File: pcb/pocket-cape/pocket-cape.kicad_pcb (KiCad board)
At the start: 4 copper layers, 49 x 32.1 mm, 28 parts, among them J1 Sync1, J10 Display, J11 USB1, J2 12..16V, J3 Sync2, J4 Sled, J5 Laser1, J6 PM1, J7 PM2, J8 Laser2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

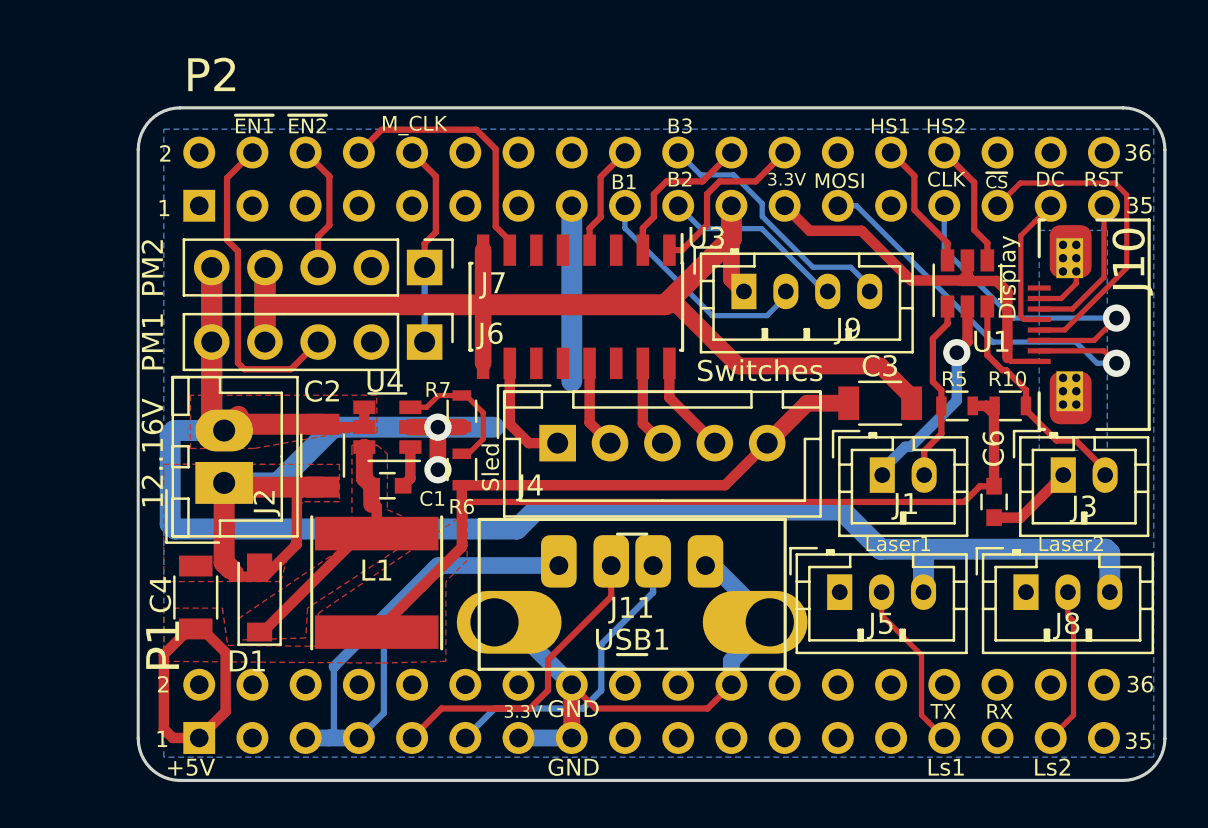
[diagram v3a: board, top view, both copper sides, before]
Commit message: Little tweaks (silk-screen; adding 100nF on 3.3V rail)
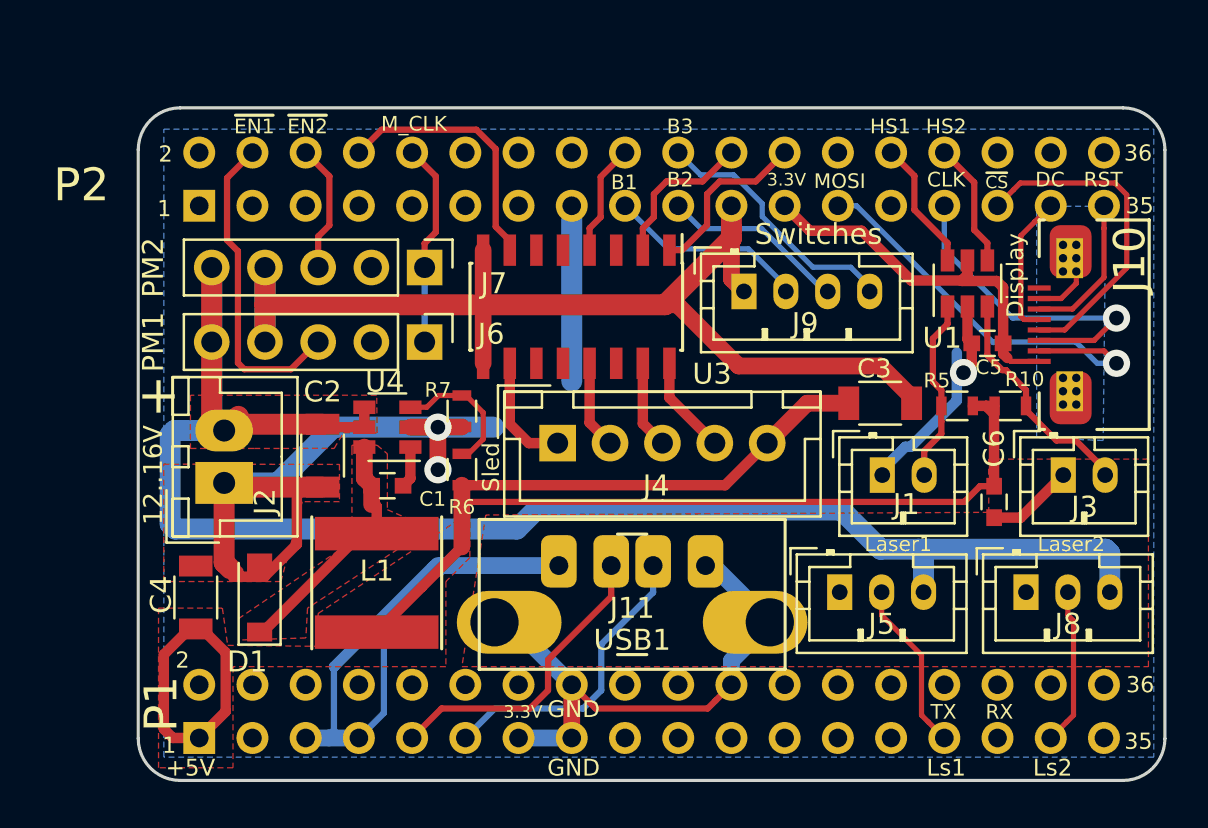
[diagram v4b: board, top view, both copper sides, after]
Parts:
- removed the REF*** at (148.5, 97.8)
- added C5: 100n, Capacitors_SMD:C_0603, F.Cu at (164.5, 100.1)
- added REF***: OSHW-Symbol_6.7x6mm_SilkScreen, Symbols:OSHW-Symbol_6.7x6mm_SilkScreen, B.Cu at (148.5, 97.9)
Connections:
- J10 pad 8: (no net) -> Net-(J10-Pad8)
- J6 pad 2: Net-(J6-Pad2) -> (no net)
- J7 pad 2: Net-(J7-Pad2) -> (no net)
- P1 pad 10: /(U1.B13)SPI0.MISO -> (no net)
- P1 pad 12: /(U1.B14)SPI0.MOSI -> (no net)
- P1 pad 14: (no net) -> Net-(P1-Pad14)
- P1 pad 17: /(U1.B9)VREF- -> (no net)
- P1 pad 18: /(U1.B7)VREF+ -> (no net)
- P1 pad 19: /(U1.A8)AIN0~1.8V -> (no net)
- P1 pad 2: /(U1.F2)AIN6~3.3V -> (no net)
- P1 pad 20: /(U1.B4)PRU-0.16 -> (no net)
- P1 pad 21: /(U1.B8)AIN1~1.8V -> (no net)
- P1 pad 23: /(U1.B6)AIN2~1.8V -> (no net)
- P1 pad 24: (no net) -> Net-(P1-Pad24)
- P1 pad 25: /(U1.C6)AIN3~1.8V -> (no net)
- P1 pad 26: /(U1.B10)I2C2.SDA -> (no net)
- P1 pad 27: /(U1.C7)AIN4~1.8V -> (no net)
- P1 pad 28: /(U1.A10)I2C2.SCL -> (no net)
- P1 pad 3: /(U1.M14)USB1.DRVVBUS -> (no net)
- P1 pad 30: /(U1.B12)UART0.TX -> (no net)
- P1 pad 31: /(U1.A3)PRU-0.4 -> (no net)
- P1 pad 32: /(U1.A12)UART0.RX -> (no net)
- P1 pad 34: /(U1.R5)GPIO-0.26 -> (no net)
- P1 pad 35: /(U1.F1) -> (no net)
- P1 pad 36: /(U1.A1)PWM0A -> (no net)
- P1 pad 4: /(U1.E1) -> (no net)
- P1 pad 6: /(U1.A14)SPI0.CS -> (no net)
- P1 pad 8: /(U1.A13)SPI0.CLK -> (no net)
- P2 pad 1: /(U1.P12)PWM1A -> (no net)
- P2 pad 11: /(U1.A11)I2C1.SDA -> (no net)
- P2 pad 12: /(U1.T11)PWR.BTN -> (no net)
- P2 pad 13: SYS_5V -> (no net)
- P2 pad 14: VIN.BAT -> (no net)
- P2 pad 16: /BAT.TEMP -> (no net)
- P2 pad 2: /(U1.T16) -> (no net)
- P2 pad 26: /(U1.R11)RESET# -> (no net)
- P2 pad 27: /(U1.C12)SPI1.MISO -> (no net)
- P2 pad 3: /(U1.P5)GPIO-0.23 -> (no net)
- P2 pad 32: /(U1.B2)PRU-0.2 -> (no net)
- P2 pad 34: /(U1.B3)PRU-0.5 -> (no net)
- P2 pad 36: /(U1.N13)AIN7~1.8V -> (no net)
- P2 pad 5: /(U1.P15)UART4.RX -> (no net)
- P2 pad 7: /(U1.R16)UART4.TX -> (no net)
- P2 pad 9: /(U1.B11)I2C1.SCL -> (no net)
- U3 pad 11: (no net) -> Net-(U3-Pad11)
- U3 pad 12: (no net) -> Net-(U3-Pad12)
- U3 pad 14: (no net) -> Net-(U3-Pad14)
- U3 pad 3: (no net) -> Net-(U3-Pad3)
- U3 pad 5: (no net) -> Net-(U3-Pad5)
- U3 pad 6: (no net) -> Net-(U3-Pad6)
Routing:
- net BUTT_1: track 11.1 -> 9.77 mm
- net GND: track 144.8 -> 145.8 mm
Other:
- board text added: "+"

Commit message: Get 0.2mm clearance throughout.
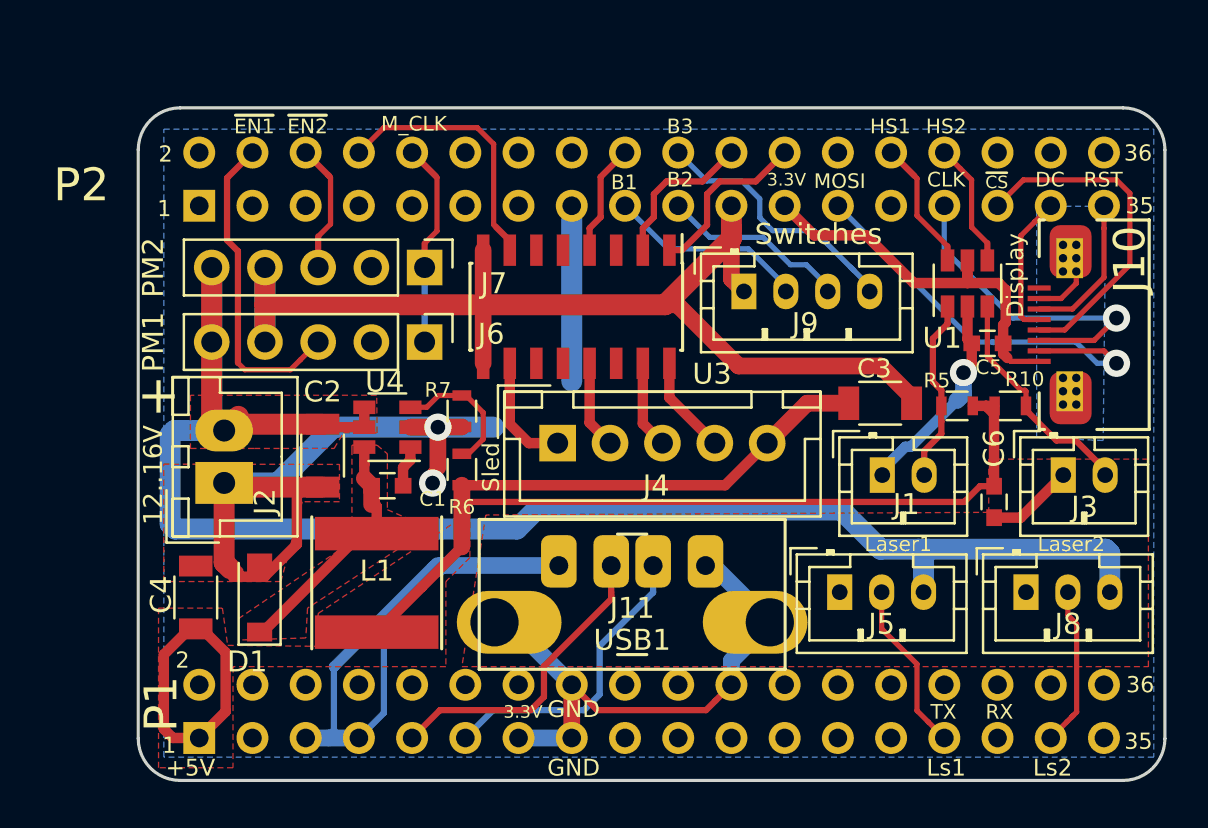
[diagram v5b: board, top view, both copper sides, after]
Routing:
- net BUTT_2: track 8.83 -> 9.33 mm
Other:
- net class Default: clearance 0.18 -> 0.2
- rule trace_clearance: 0.18 -> 0.2
